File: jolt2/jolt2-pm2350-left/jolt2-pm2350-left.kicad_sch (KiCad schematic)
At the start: 5 parts, among them J29 RJ45

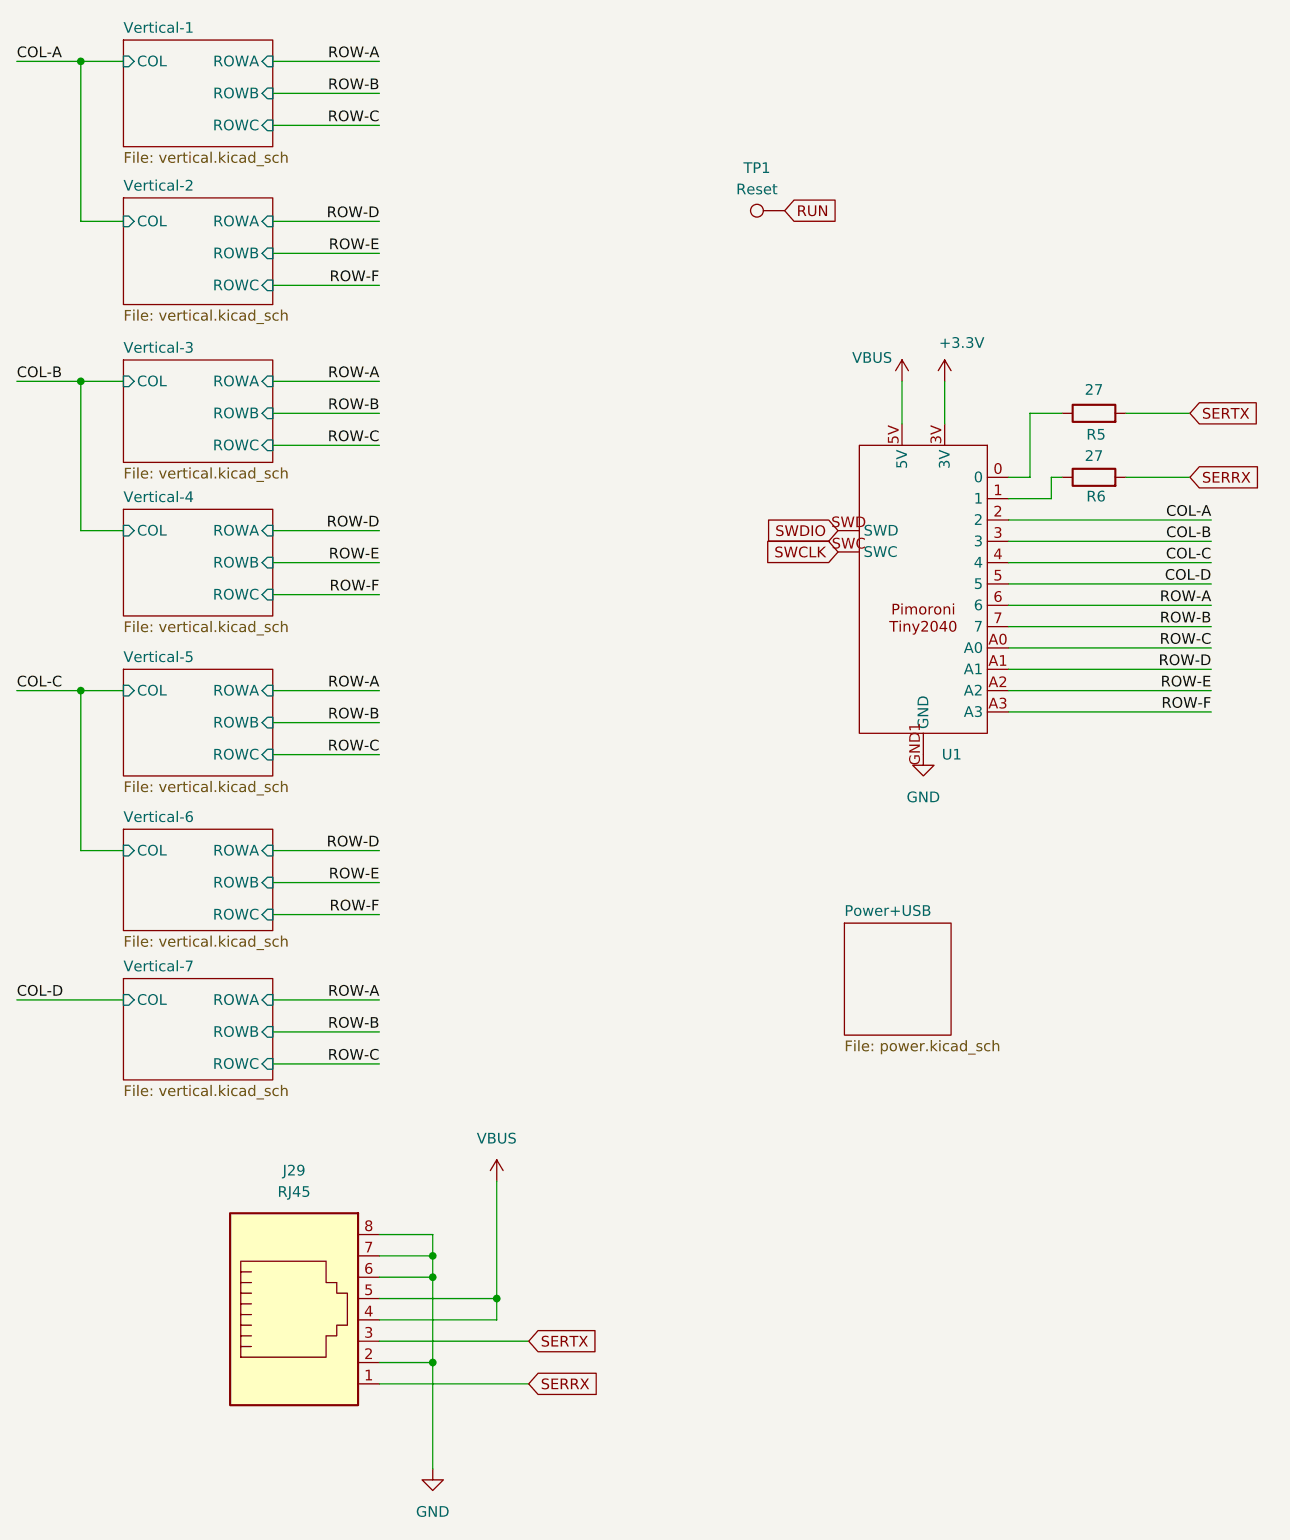
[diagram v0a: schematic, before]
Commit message: jolt2: Update pm2350 left footprint
Build the footprint, updating it for the left side of the keyboard
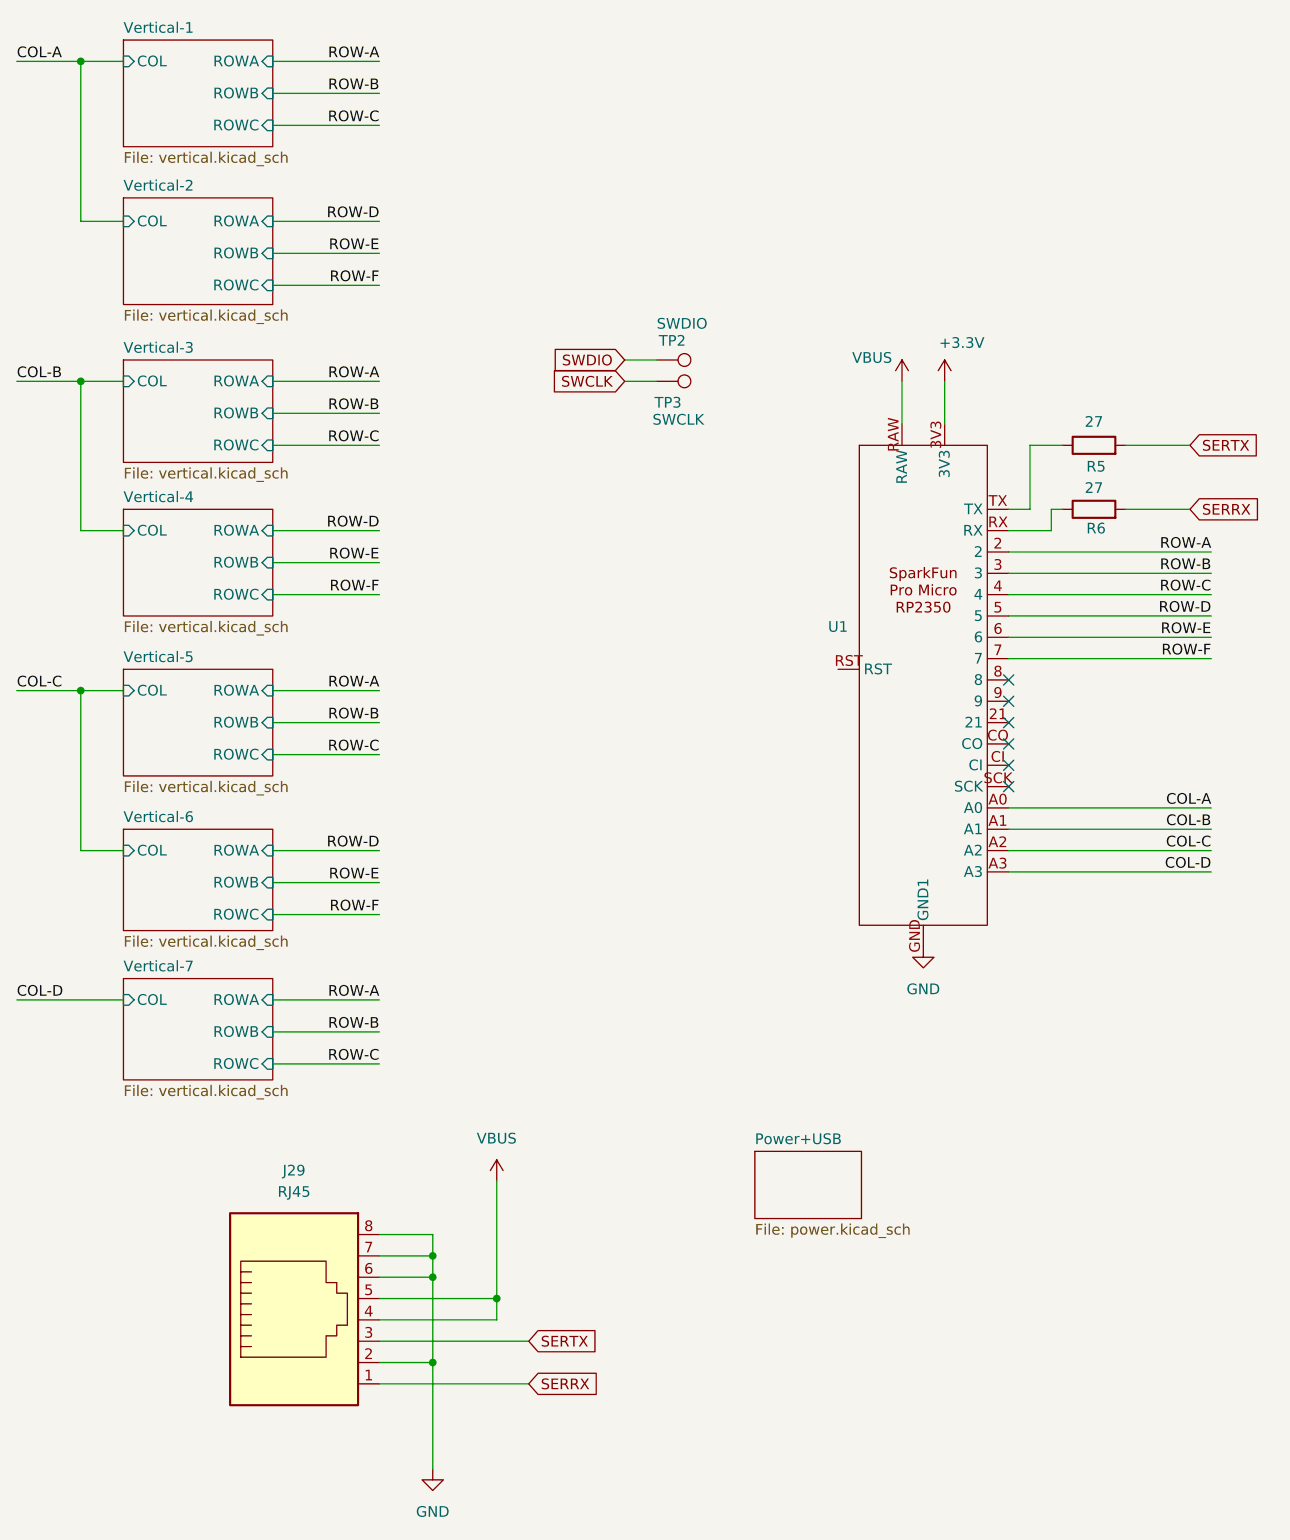
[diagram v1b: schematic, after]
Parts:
- removed TP1: Reset, TestPoint:TestPoint_Pad_2.0x2.0mm, symbol Connector:TestPoint
- removed U1: ~, davidb-keyboard-foot:Pimoroni-Tiny2040, symbol David Brown Keyboard Parts:Pimoroni-Tiny2040
- added TP2: SWDIO, TestPoint:TestPoint_Pad_1.5x1.5mm, symbol Connector:TestPoint
- added TP3: SWCLK, TestPoint:TestPoint_Pad_1.5x1.5mm, symbol Connector:TestPoint
- added U1: ~, davidb-keyboard-foot:SparkFun_Pro_Micro_RP2350, symbol David Brown Keyboard Parts:SparkFun_Pro_Micro_RP2350
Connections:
- net +3.3V: now also U1.3V3
- net COL-A: now also U1.A0
- net COL-B: now also U1.A1
- net COL-C: now also U1.A2
- net COL-D: now also U1.A3
- net GND: now also U1.GND (GND2)
- net ROW-A: now also U1.2
- net ROW-B: now also U1.3
- net ROW-C: now also U1.4
- net ROW-D: now also U1.5
- net ROW-E: now also U1.6
- net ROW-F: now also U1.7
- net SWCLK: now also TP3.1
- net SWDIO: now also TP2.1
- net VBUS: now also U1.RAW
- net at R5.1: now also U1.TX
- net at R6.1: now also U1.RX
- no-connect marks 0 -> 6
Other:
- moved on the sheet: R5, R6
